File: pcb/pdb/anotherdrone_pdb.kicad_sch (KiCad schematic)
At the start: 28 parts, among them J1 BATT, J10 STAT, J11 MCU, J12 5v, J3 3v, J6 ESC A, J7 ESC B, J8 ESC C, J9 ESC D, P1 ESC Power A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

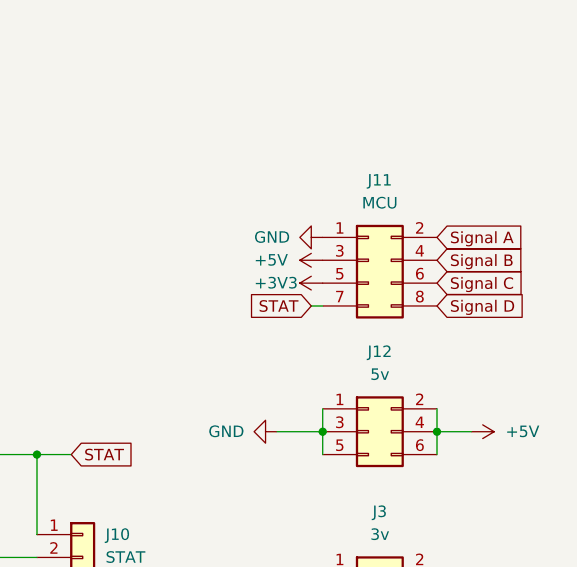
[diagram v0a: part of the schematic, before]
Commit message: now using 15v and ground planes
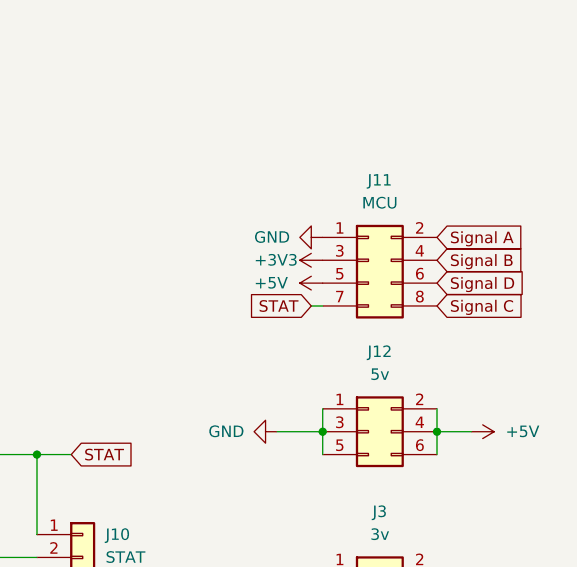
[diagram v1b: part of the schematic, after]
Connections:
- net +3V3: now also J11.3 (Pin_3); no longer J11.5 (Pin_5)
- net +5V: now also J11.5 (Pin_5); no longer J11.3 (Pin_3)
- net Signal C: now also J11.8 (Pin_8); no longer J11.6 (Pin_6)
- net Signal D: now also J11.6 (Pin_6); no longer J11.8 (Pin_8)
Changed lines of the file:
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@@
     )
   )
-  (global_label "Signal C" (shape input) (at 179.07 58.42 0) (fields_autoplaced)
+  (global_label "Signal C" (shape input) (at 179.07 60.96 0) (fields_autoplaced)
+    (effects (font (size 1.27 1.27)) (justify left))
+    (property "Intersheet References" "${INTERSHEET_REFS}" (id 0) (at 189.6474 60.8806 0)
+      (effects (font (size 1.27 1.27)) (justify left) hide)
+    )
+  )
+  (global_label "Signal D" (shape input) (at 179.07 58.42 0) (fields_autoplaced)
     (effects (font (size 1.27 1.27)) (justify left))
     (property "Intersheet References" "${INTERSHEET_REFS}" (id 0) (at 189.6474 58.3406 0)
-      (effects (font (size 1.27 1.27)) (justify left) hide)
-    )
-  )
-  (global_label "Signal D" (shape input) (at 179.07 60.96 0) (fields_autoplaced)
-    (effects (font (size 1.27 1.27)) (justify left))
-    (property "Intersheet References" "${INTERSHEET_REFS}" (id 0) (at 189.6474 60.8806 0)
       (effects (font (size 1.27 1.27)) (justify left) hide)
     )
@@
     (pin "2")
   )
+  (symbol (lib_id "power:+5V") (at 166.37 58.42 90) (mirror x) (unit 1)
+    (in_bom yes) (on_board yes)
+    (property "Reference" "#PWR?" (id 0) (at 170.18 58.42 0)
+      (effects (font (size 1.27 1.27)) hide)
+    )
+    (property "Value" "+5V" (id 1) (at 158.75 58.42 90)
+      (effects (font (size 1.27 1.27)) (justify right))
+    )
+    (property "Footprint" "" (id 2) (at 166.37 58.42 0)
+      (effects (font (size 1.27 1.27)) hide)
+    )
+    (property "Datasheet" "" (id 3) (at 166.37 58.42 0)
+      (effects (font (size 1.27 1.27)) hide)
+    )
+    (pin "1")
+  )
   (symbol (lib_id "Device:LED") (at 21.59 120.65 90) (unit 1)
     (in_bom yes) (on_board yes) (fields_autoplaced)
@@
     (pin "1")
     (pin "2")
-  )
-  (symbol (lib_id "power:+5V") (at 166.37 55.88 90) (mirror x) (unit 1)
-    (in_bom yes) (on_board yes)
-    (property "Reference" "#PWR0107" (id 0) (at 170.18 55.88 0)
-      (effects (font (size 1.27 1.27)) hide)
-    )
-    (property "Value" "+5V" (id 1) (at 158.75 55.88 90)
-      (effects (font (size 1.27 1.27)) (justify right))
-    )
-    (property "Footprint" "" (id 2) (at 166.37 55.88 0)
-      (effects (font (size 1.27 1.27)) hide)
-    )
-    (property "Datasheet" "" (id 3) (at 166.37 55.88 0)
-      (effects (font (size 1.27 1.27)) hide)
-    )
-    (pin "1")
   )
   (symbol (lib_id "Connector_Generic:Conn_01x02") (at 139.7 86.36 0) (unit 1)
@@
     (pin "2")
   )
-  (symbol (lib_id "power:+3V3") (at 166.37 58.42 90) (mirror x) (unit 1)
-    (in_bom yes) (on_board yes)
-    (property "Reference" "#PWR0105" (id 0) (at 170.18 58.42 0)
-      (effects (font (size 1.27 1.27)) hide)
-    )
-    (property "Value" "+3V3" (id 1) (at 158.75 58.42 90)
-      (effects (font (size 1.27 1.27)) (justify right))
-    )
-    (property "Footprint" "" (id 2) (at 166.37 58.42 0)
-      (effects (font (size 1.27 1.27)) hide)
-    )
-    (property "Datasheet" "" (id 3) (at 166.37 58.42 0)
-      (effects (font (size 1.27 1.27)) hide)
-    )
-    (pin "1")
-  )
   (symbol (lib_id "power:GND") (at 45.72 121.92 0) (mirror x) (unit 1)
     (in_bom yes) (on_board yes)
@@
     (pin "2")
   )
+  (symbol (lib_id "power:+3V3") (at 166.37 55.88 90) (mirror x) (unit 1)
+    (in_bom yes) (on_board yes)
+    (property "Reference" "#PWR?" (id 0) (at 170.18 55.88 0)
+      (effects (font (size 1.27 1.27)) hide)
+    )
+    (property "Value" "+3V3" (id 1) (at 158.75 55.88 90)
+      (effects (font (size 1.27 1.27)) (justify right))
+    )
+    (property "Footprint" "" (id 2) (at 166.37 55.88 0)
+      (effects (font (size 1.27 1.27)) hide)
+    )
+    (property "Datasheet" "" (id 3) (at 166.37 55.88 0)
+      (effects (font (size 1.27 1.27)) hide)
+    )
+    (pin "1")
+  )
   (symbol (lib_id "Device:C_Polarized") (at 101.6 35.56 0) (unit 1)
     (in_bom yes) (on_board yes) (fields_autoplaced)
@@
       (reference "#PWR0102") (unit 1) (value "+15V") (footprint "")
     )
-    (path "/a5f978fa-324c-4321-9e80-d3b16cb23e08"
-      (reference "#PWR0105") (unit 1) (value "+3V3") (footprint "")
-    )
     (path "/9bdb52dd-f460-4b80-977d-998c758b3e8a"
       (reference "#PWR0106") (unit 1) (value "GND") (footprint "")
     )
-    (path "/52b70ebc-6716-48bd-ada1-df7ec252b3ad"
-      (reference "#PWR0107") (unit 1) (value "+5V") (footprint "")
-    )
     (path "/9fa69bcb-18b0-4d4b-92de-8e676cea1785"
       (reference "#PWR0109") (unit 1) (value "+15V") (footprint "")
@@
       (reference "#PWR0121") (unit 1) (value "+15V") (footprint "")
     )
+    (path "/36a8c8f5-482b-4338-8116-1a3cb6257541"
+      (reference "#PWR?") (unit 1) (value "+5V") (footprint "")
+    )
+    (path "/e11c6922-fb16-49b0-8ede-7ae45eb548f0"
+      (reference "#PWR?") (unit 1) (value "+3V3") (footprint "")
+    )
     (path "/cc504aef-8779-4d05-ac3a-b4e6d553d16f"
